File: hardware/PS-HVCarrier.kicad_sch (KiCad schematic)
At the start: 4 parts, among them J2 IMD_Conn, J3 LEM CAB 500-C

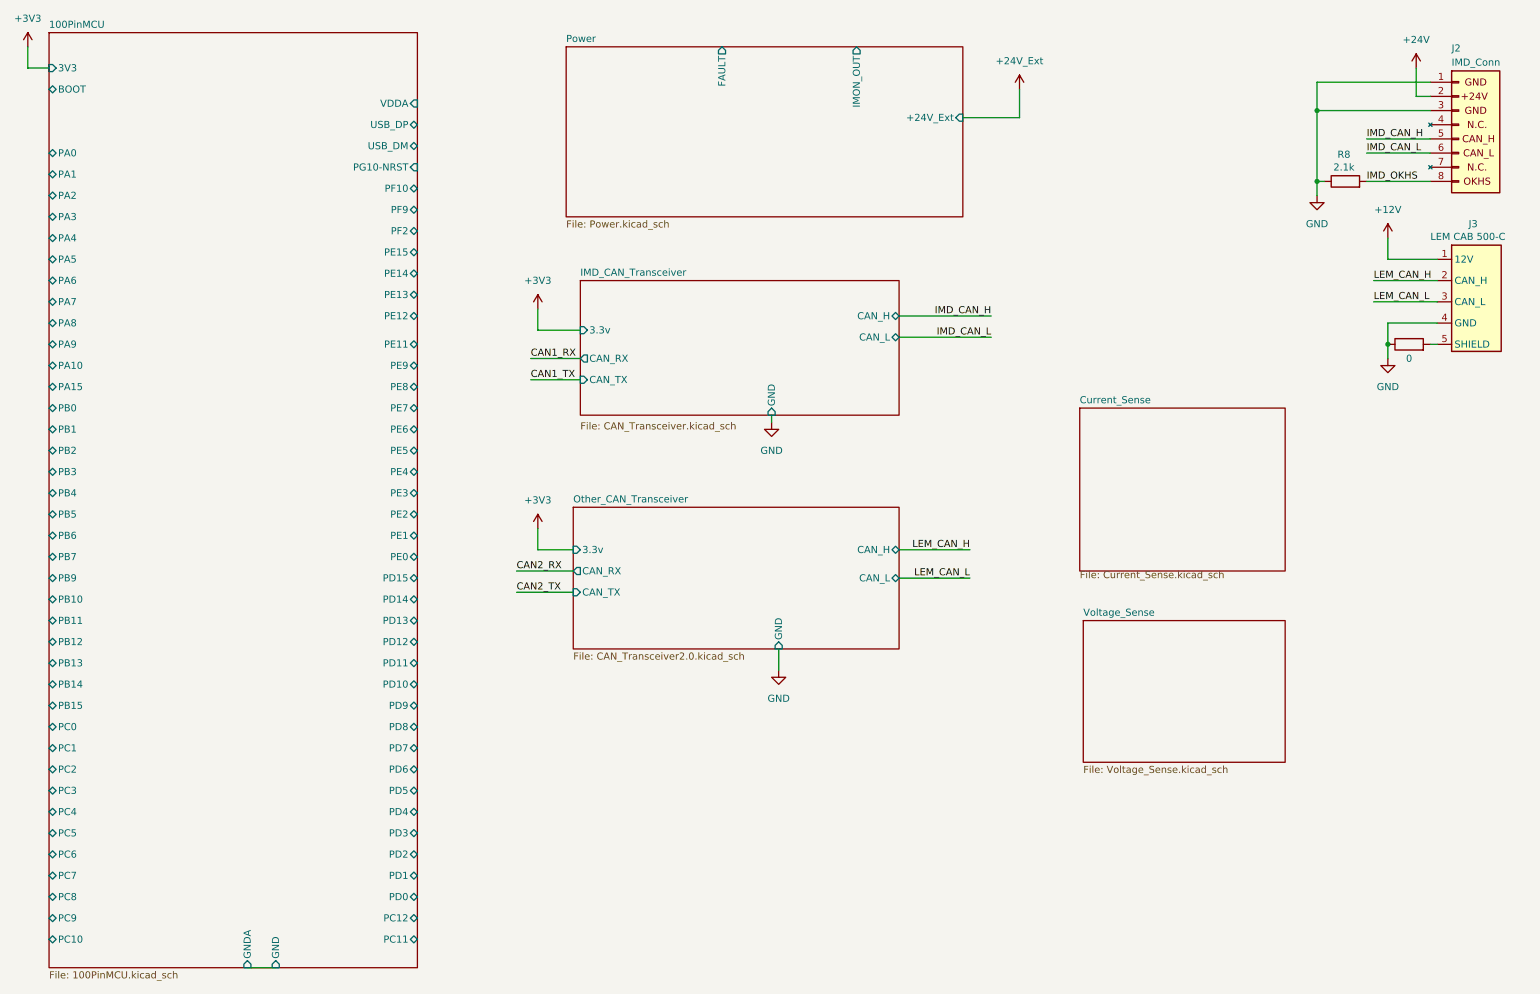
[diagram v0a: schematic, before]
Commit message: added designs for LZSR-80P and AMC class voltage sense
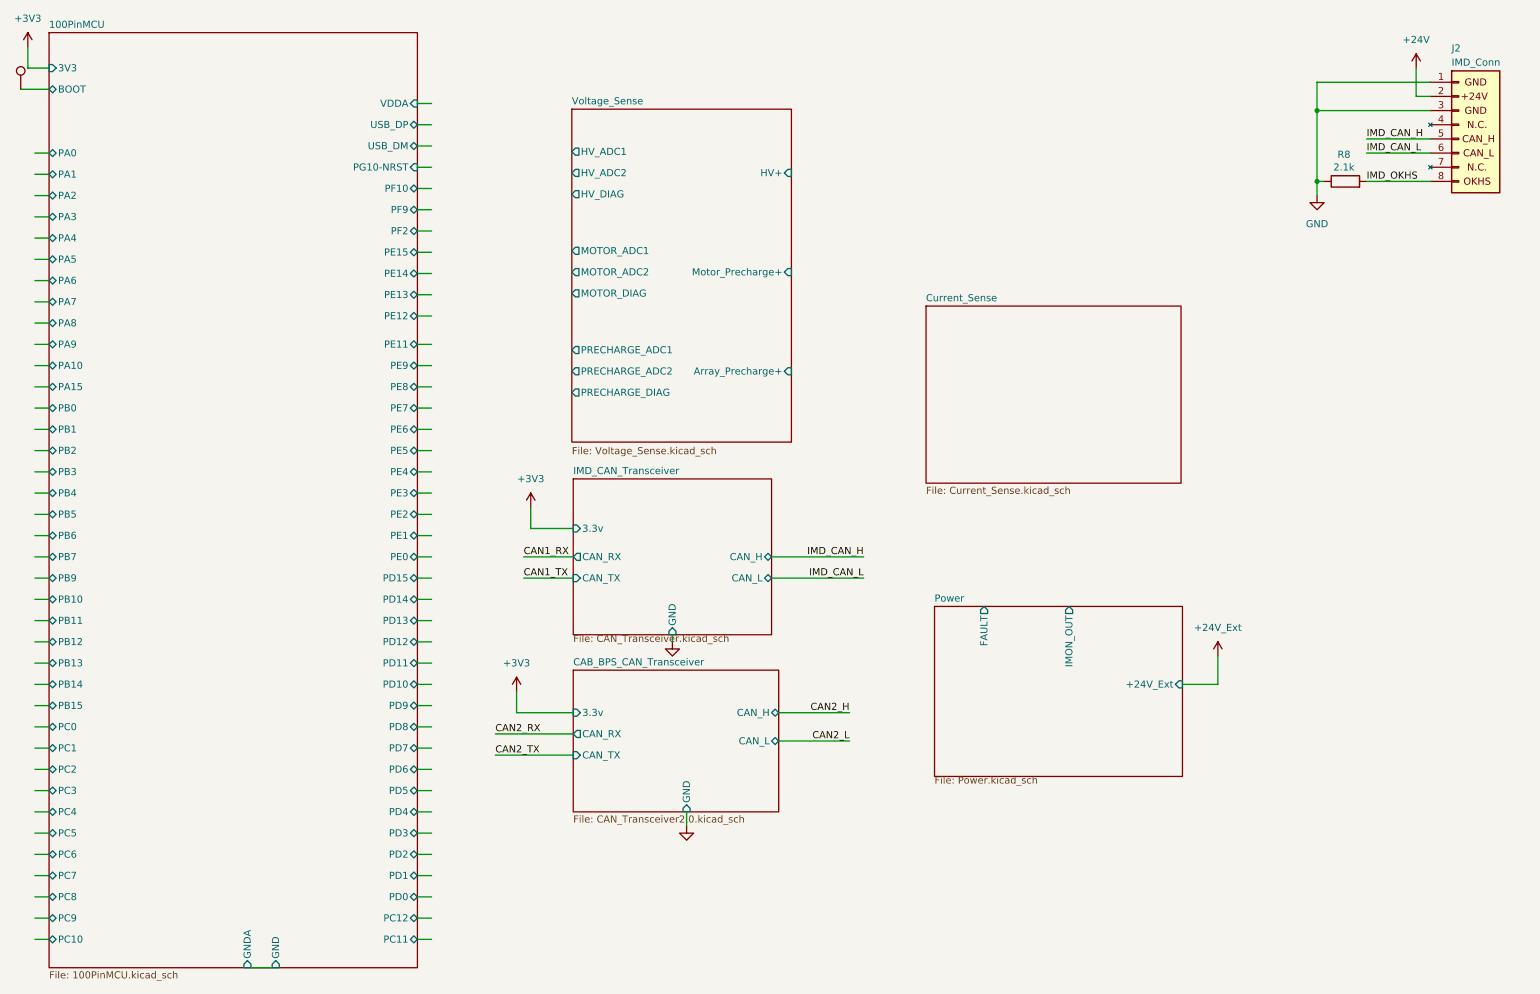
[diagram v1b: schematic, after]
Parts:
- removed J3: LEM CAB 500-C, LHRS_Connectors:Molex_Nano-Fit_105309-xx05_1x05_P2.50mm_Vertical, symbol lhrs_connectors:CAN_NANO_01x05
- removed R6: 0, symbol Device:R
- added TP1: TestPoint, symbol Connector:TestPoint
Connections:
- net 100PinMCU/BOOT: now also TP1.1
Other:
- sheet Other_CAN_Transceiver renamed CAB_BPS_CAN_Transceiver
- sheet Voltage_Sense ports: added Array_Precharge+, HV+, HV_ADC1, HV_ADC2, HV_DIAG, MOTOR_ADC1, MOTOR_ADC2, MOTOR_DIAG, Motor_Precharge+, PRECHARGE_ADC1, PRECHARGE_ADC2, PRECHARGE_DIAG; removed none
